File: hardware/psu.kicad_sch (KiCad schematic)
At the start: 58 parts, among them IC1 TLV61220DBVT, J2 Conn_01x03, J6 Barrel_Jack_Switch, Q3 CSD87503Q3E, Q4 CSD87503Q3E, U4 TPS63020DSJR, U5 BQ25798RQMR

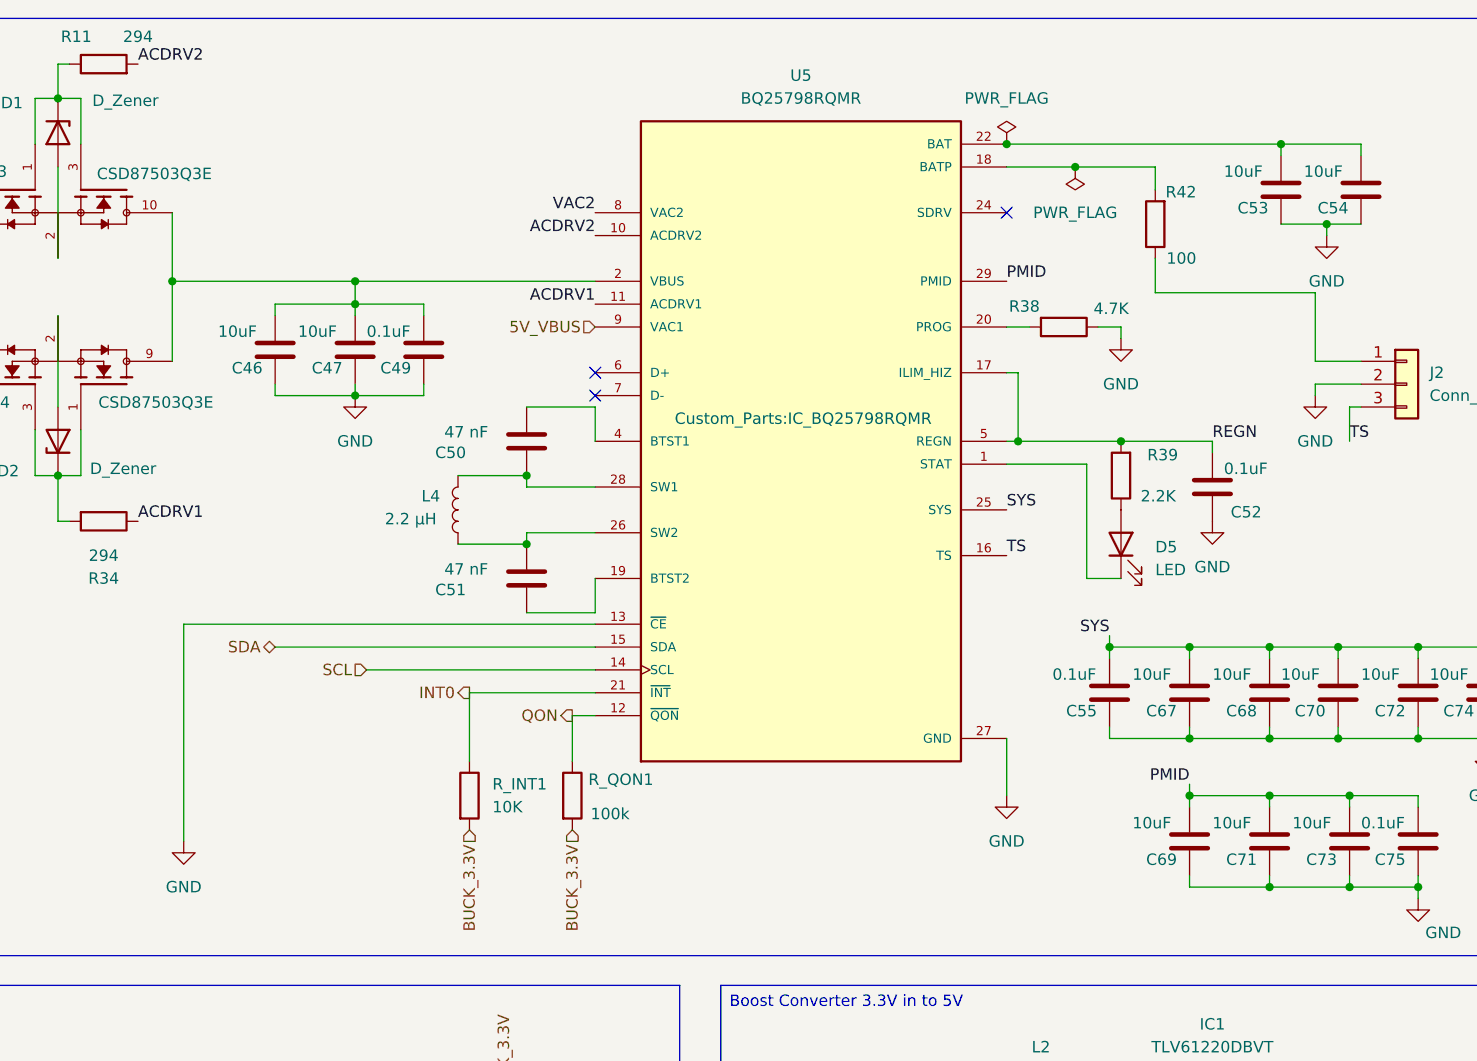
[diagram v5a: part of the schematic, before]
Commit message: Fixed MCU JTAG/Reordered pages
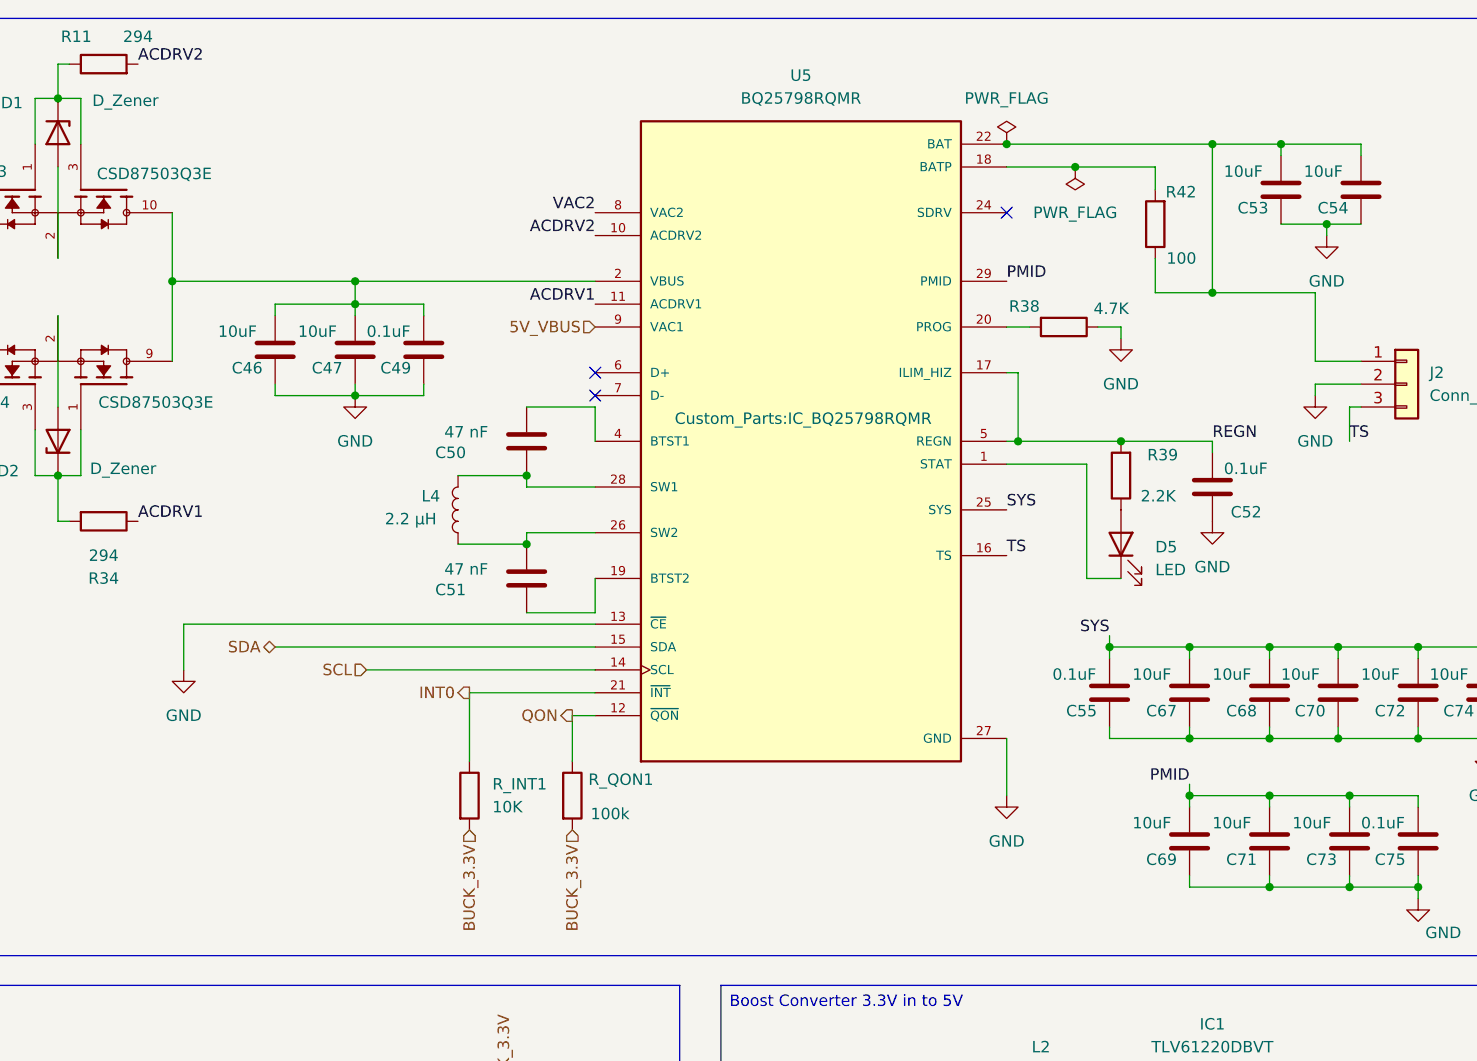
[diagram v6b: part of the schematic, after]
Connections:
- net BAT: now also J2.1 (Pin_1), R42.1
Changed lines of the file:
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@@
 	)
 	(junction
+		(at 199.39 27.94)
+		(diameter 0)
+		(color 0 0 0 0)
+	)
+	(junction
 		(at 196.85 83.82)
 		(diameter 0)
@@
 	)
 	(junction
+		(at 199.39 44.45)
+		(diameter 0)
+		(color 0 0 0 0)
+	)
+	(junction
 		(at 218.44 147.32)
 		(diameter 0)
@@
 	(wire
 		(pts
-			(xy 193.04 44.45) (xy 210.82 44.45)
+			(xy 193.04 44.45) (xy 199.39 44.45)
 		)
 		(stroke
@@
 	(wire
 		(pts
-			(xy 85.09 81.28) (xy 85.09 105.41)
+			(xy 85.09 81.28) (xy 85.09 86.36)
 		)
 		(stroke
@@
 	(wire
 		(pts
+			(xy 199.39 44.45) (xy 210.82 44.45)
+		)
+		(stroke
+			(width 0)
+			(type default)
+		)
+	)
+	(wire
+		(pts
 			(xy 73.66 22.86) (xy 71.12 22.86)
 		)
@@
 	(wire
 		(pts
+			(xy 199.39 27.94) (xy 207.01 27.94)
+		)
+		(stroke
+			(width 0)
+			(type default)
+		)
+	)
+	(wire
+		(pts
 			(xy 212.09 36.83) (xy 212.09 38.1)
 		)
@@
 	(wire
 		(pts
-			(xy 176.53 27.94) (xy 207.01 27.94)
+			(xy 176.53 27.94) (xy 199.39 27.94)
 		)
 		(stroke
@@
 		)
 	)
+	(wire
+		(pts
+			(xy 199.39 27.94) (xy 199.39 44.45)
+		)
+		(stroke
+			(width 0)
+			(type default)
+		)
+	)
 	(label "SYS"
 		(at 187.96 82.55 180)
@@
 	(symbol
 		(lib_id "power:GND")
-		(at 85.09 105.41 0)
+		(at 85.09 86.36 0)
 		(unit 1)
 		(exclude_from_sim no)
@@
 		(fields_autoplaced yes)
 		(property "Reference" "#PWR039"
-			(at 85.09 111.76 0)
+			(at 85.09 92.71 0)
 			(effects
 				(font
@@
 		)
 		(property "Value" "GND"
-			(at 85.09 110.49 0)
+			(at 85.09 91.44 0)
 			(effects
 				(font
@@
 		)
 		(property "Footprint" ""
-			(at 85.09 105.41 0)
+			(at 85.09 86.36 0)
 			(effects
 				(font
@@
 		)
 		(property "Datasheet" ""
-			(at 85.09 105.41 0)
+			(at 85.09 86.36 0)
 			(effects
 				(font
@@
 		)
 		(property "Description" "Power symbol creates a global label with name \"GND\" , ground"
-			(at 85.09 105.41 0)
+			(at 85.09 86.36 0)
 			(effects
 				(font

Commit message: cleanup
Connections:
- net VINPUT is gone; now on net BUCK_3.3V: C26.1, IC1.3 (EN), IC1.6 (VBAT), L2.1
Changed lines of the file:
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@@
 	(wire
 		(pts
-			(xy 156.21 138.43) (xy 170.18 138.43)
+			(xy 158.75 138.43) (xy 170.18 138.43)
 		)
 		(stroke
@@
 			)
 			(justify right bottom)
-		)
-	)
-	(global_label "VINPUT"
-		(shape input)
-		(at 156.21 138.43 180)
-		(fields_autoplaced yes)
-		(effects
-			(font
-				(size 1.27 1.27)
-			)
-			(justify right)
-		)
-		(property "Intersheetrefs" "${INTERSHEET_REFS}"
-			(at 146.6328 138.43 0)
-			(effects
-				(font
-					(size 1.27 1.27)
-				)
-				(justify right)
-				(hide yes)
-			)
 		)
 	)
@@
 		(effects
 			(font
+				(size 1.27 1.27)
+			)
+			(justify right)
+		)
+	)
+	(hierarchical_label "BUCK_3.3V"
+		(shape input)
+		(at 158.75 138.43 180)
+		(effects
+			(font

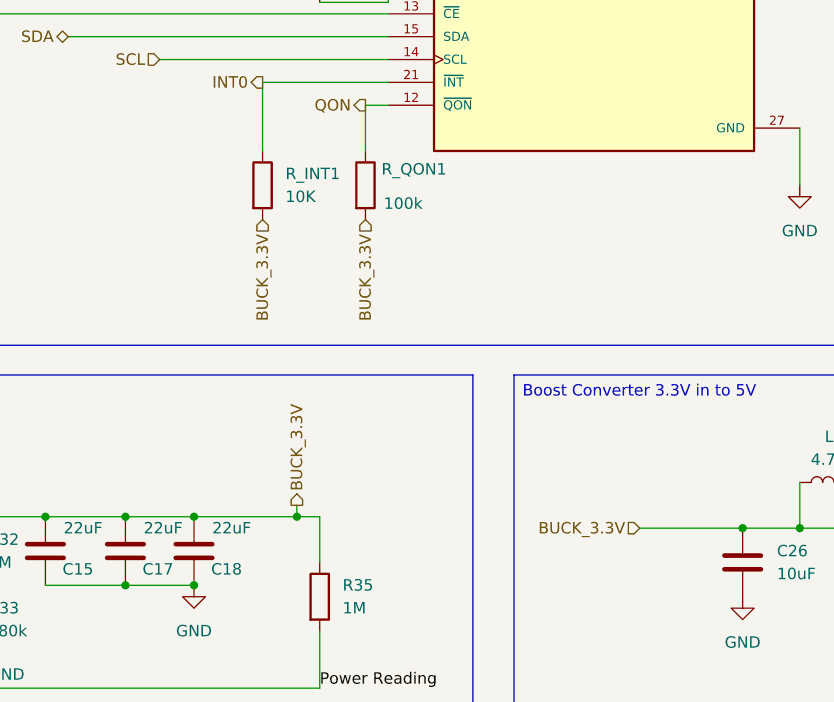
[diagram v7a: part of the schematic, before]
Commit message: Replaced 3.3V symbol
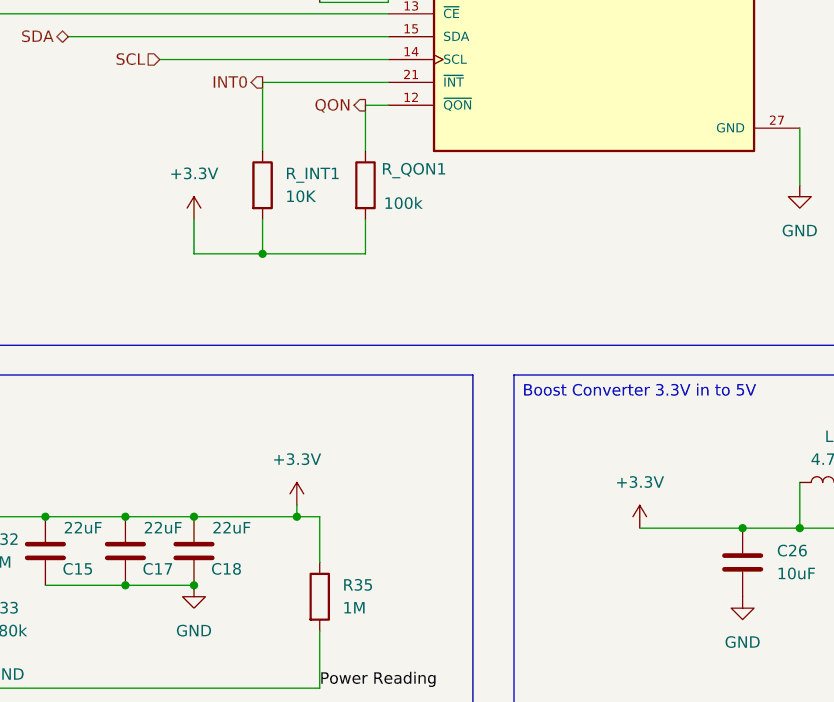
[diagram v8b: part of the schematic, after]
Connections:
- net BUCK_3.3V renamed +3.3V
